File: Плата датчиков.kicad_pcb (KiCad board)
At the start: 4 copper layers, 67 x 68.5 mm, 51 parts, among them J1 A, J10 4900, J11 4900, J12 4900, J13 4900, J14 4900, J2 B, J3 C, J4 Conn_02x07_Odd_Even, J5 4900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

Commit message: Собираю документацию
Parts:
- added R15: 9.1k, Resistor_SMD:R_0603_1608Metric_Pad0.98x0.95mm_HandSolder, F.Cu at (81.5, 107.4)
- added R16: 1k, Resistor_SMD:R_0603_1608Metric_Pad0.98x0.95mm_HandSolder, F.Cu at (80.0, 107.4)
- added R17: 1k, Resistor_SMD:R_0603_1608Metric_Pad0.98x0.95mm_HandSolder, F.Cu at (80.0, 112.3)
- added R18: 1k, Resistor_SMD:R_0603_1608Metric_Pad0.98x0.95mm_HandSolder, F.Cu at (94.2, 107.2)
- added R19: 9.1k, Resistor_SMD:R_0603_1608Metric_Pad0.98x0.95mm_HandSolder, F.Cu at (92.7, 107.2)
- added R20: 9.1k, Resistor_SMD:R_0603_1608Metric_Pad0.98x0.95mm_HandSolder, F.Cu at (81.5, 112.3)
- C10, C12, C14: value 100n -> 1u
- R11, R13, R9: value 1.5k -> 15k
- moved J8 35.1 mm to (96.0, 114.6), turned to 0 degrees
- moved R14 33.8 mm to (83.3, 116.6), turned to 90 degrees
- moved C17 33.8 mm to (83.3, 116.6), turned to 90 degrees
- moved C14 31.2 mm to (85.9, 116.6), turned to -90 degrees
- moved R13 31.2 mm to (85.9, 116.6), turned to 90 degrees
- moved R3 27.0 mm to (94.0, 80.9)
- moved U1 27.0 mm to (97.5, 82.8)
- moved C16 27.0 mm to (94.0, 84.7)
- moved C15 26.8 mm to (97.0, 78.2)
- moved J9 26.3 mm to (109.7, 100.6), turned to 180 degrees
- moved R12 25.8 mm to (83.3, 105.4), turned to -90 degrees
- moved C18 24.9 mm to (85.9, 111.0), turned to -90 degrees
- moved J5 24.8 mm to (109.7, 96.3), turned to 180 degrees
- moved U4 24.7 mm to (87.1, 111.0), turned to -90 degrees
- moved R4 24.1 mm to (107.4, 88.6), turned to 0 degrees
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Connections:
- J8 pad 2: PTC_Coil_C -> GNDA
- J8 pad 3: PTC_Coil_B -> PTC_Coil_C
- J8 pad 4: GNDA -> PTC_Coil_B
- R10 pad 2: Net-(U4A--) -> Net-(R10-Pad2)
- R12 pad 2: Net-(U4B--) -> Net-(R12-Pad2)
- R14 pad 2: Net-(U4C--) -> Net-(R14-Pad2)
- U4 pad 1: Net-(U4A--) -> Net-(R10-Pad2)
- U4 pad 7: Net-(U4B--) -> Net-(R12-Pad2)
- U4 pad 8: Net-(U4C--) -> Net-(R14-Pad2)
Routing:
- net GND: track 0.00 -> 68.2 mm, vias 0 -> 4
- net +3.3VA: track 0.00 -> 51.0 mm, vias 0 -> 1
- net +3.3V: track 0.00 -> 46.8 mm, vias 0 -> 4
- net GNDA: track 0.00 -> 33.2 mm, vias 0 -> 4
- net Current_C_MCU: track 0.00 -> 33.0 mm, vias 0 -> 1
- net OUT_MCU: track 0.00 -> 28.7 mm, vias 0 -> 1
- net Temp_Coil_C_MCU: track 0.00 -> 28.4 mm, vias 0 -> 1
- net PTC_Coil_B: track 0.00 -> 24.6 mm, vias 0 -> 1
- net CS_MCU: track 0.00 -> 22.4 mm, vias 0 -> 1
- net SDIO_MCU: track 0.00 -> 22.0 mm, vias 0 -> 1
- net Current_B_MCU: track 0.00 -> 21.6 mm, vias 0 -> 1
- net SCLK_MCU: track 0.00 -> 20.2 mm, vias 0 -> 1
- net Temp_Coil_B_MCU: track 0.00 -> 18.6 mm, vias 0 -> 1
- net PTC_Coil_C: track 0.00 -> 16.1 mm, vias 0 -> 1
- net PTC_Coil_A: track 0.00 -> 15.2 mm, vias 0 -> 1
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- added copper zone on In1.Cu, net +3.3V
- added copper zone on B.Cu, net A
- added copper zone on F.Cu, net A
- added copper zone on In1.Cu, net A
- added copper zone on In2.Cu, net A
- added copper zone on B.Cu, net A_OUT
- added copper zone on F.Cu, net A_OUT
- added copper zone on In1.Cu, net A_OUT
- added copper zone on In2.Cu, net A_OUT
- added copper zone on B.Cu, net B
- added copper zone on F.Cu, net B
- added copper zone on In1.Cu, net B
- added copper zone on In2.Cu, net B
- added copper zone on B.Cu, net B_OUT
- added copper zone on F.Cu, net B_OUT
- added copper zone on In1.Cu, net B_OUT
- added copper zone on In2.Cu, net B_OUT
- added copper zone on B.Cu, net C
- added copper zone on F.Cu, net C
- added copper zone on In1.Cu, net C
- added copper zone on In2.Cu, net C
- added copper zone on B.Cu, net C_OUT
- added copper zone on F.Cu, net C_OUT
- added copper zone on In1.Cu, net C_OUT
- added copper zone on In2.Cu, net C_OUT
- added copper zone on B.Cu, net GND
- added copper zone on F.Cu, net GND
- added copper zone on In2.Cu, net GNDA

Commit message: Добавил все документы
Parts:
- moved C10 69.7 mm to (157.0, 92.7)
- moved C3 69.7 mm to (148.0, 86.5)
- moved C4 69.7 mm to (155.4, 86.5)
- moved J1 69.7 mm to (174.0, 70.5)
- moved J12 69.7 mm to (140.0, 62.1)
- moved R1 69.7 mm to (146.1, 86.5)
- moved R2 69.7 mm to (157.4, 86.5)
- moved R9 69.7 mm to (157.0, 92.7)
- moved U1 69.7 mm to (166.1, 70.1)
- moved C1 69.7 mm to (146.7, 89.1)
- moved C11 69.7 mm to (159.5, 92.7)
- moved C13 69.7 mm to (151.9, 92.7)
- moved C15 69.7 mm to (165.6, 65.5)
- moved C16 69.7 mm to (162.6, 72.0)
- moved C17 69.7 mm to (151.9, 103.9)
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
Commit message: Версия под отчёт
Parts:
- R1: value 10 -> 0
- R2: value 50 -> 51
- U1, U2, U3: value INA283 -> INA282

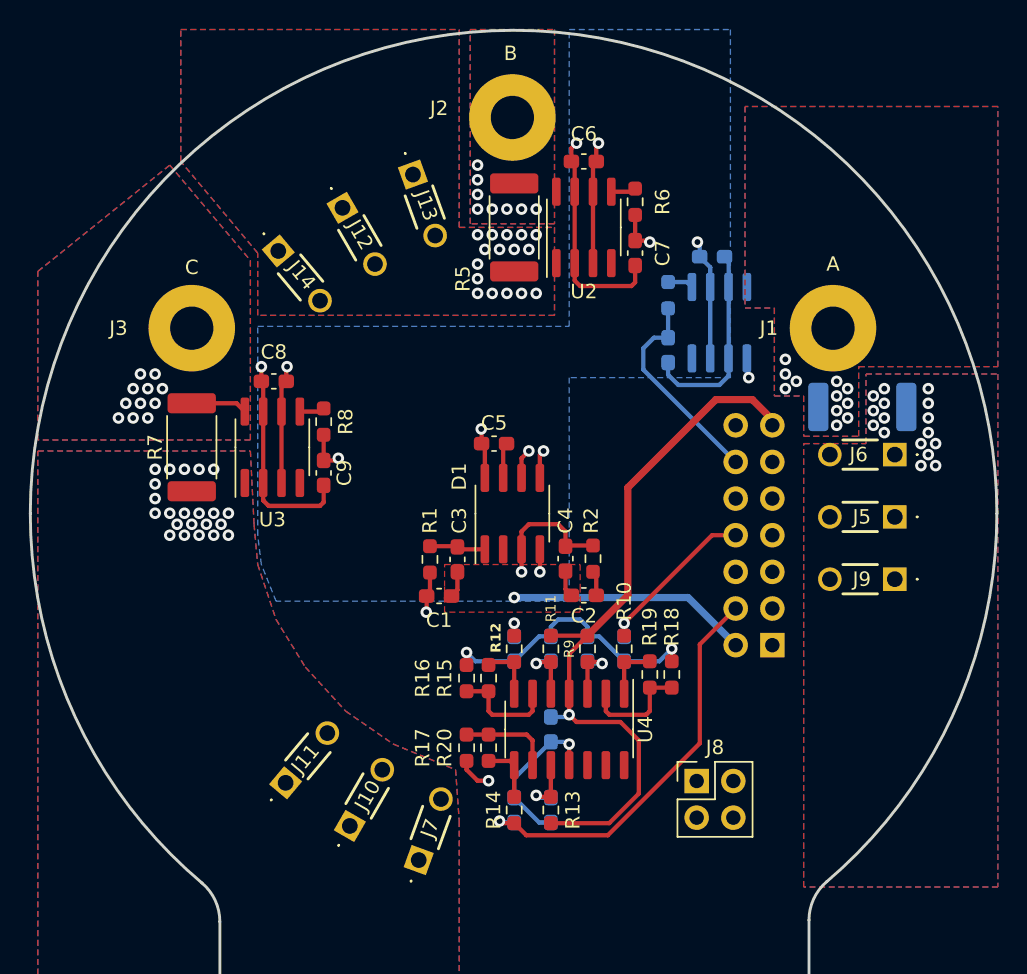
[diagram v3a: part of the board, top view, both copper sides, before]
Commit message: Изменил разводку шунтов, вывел выход датчика положения после фильтра
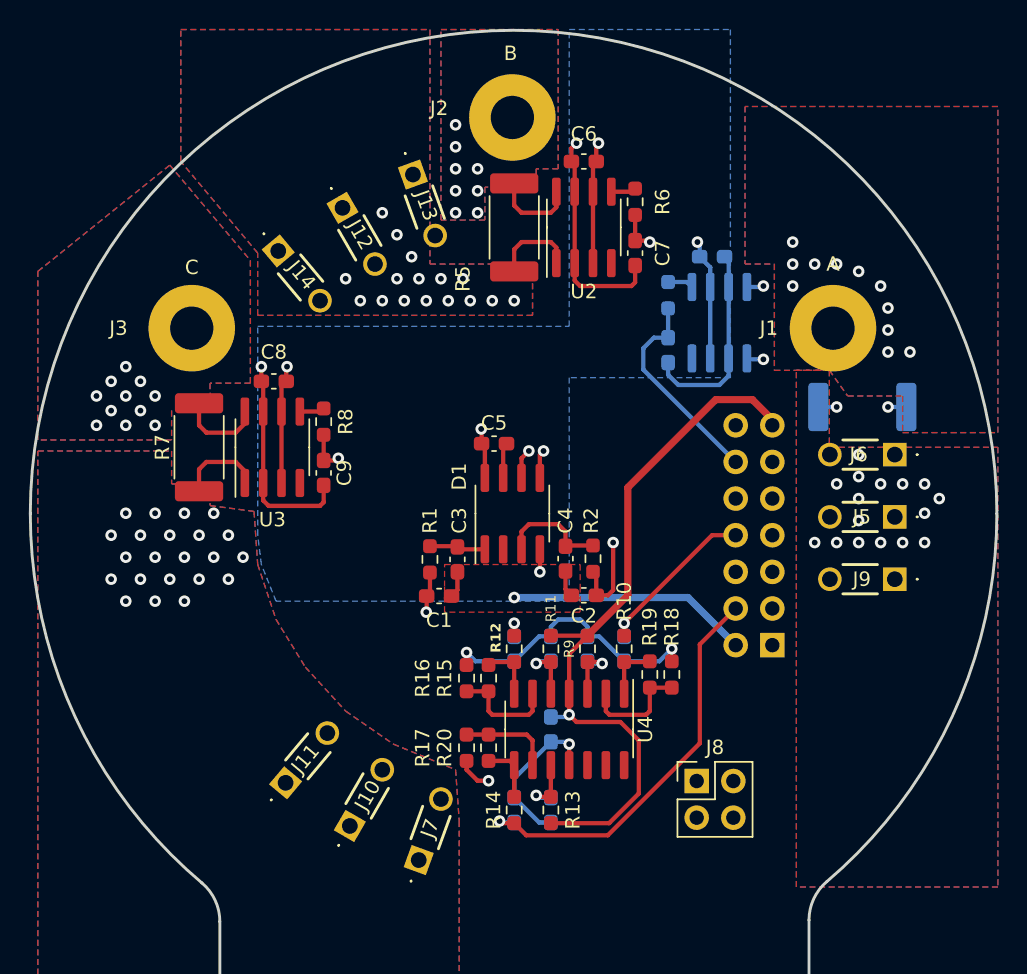
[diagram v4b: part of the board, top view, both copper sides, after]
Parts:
- moved R7 0.51 mm to (130.0, 78.7)
- turned R4 to 180 degrees
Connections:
- C2 pad 2: Net-(C2-Pad2) -> OUT_MCU
- C4 pad 2: OUT_MCU -> Net-(D1-OUT)
- D1 pad 3: OUT_MCU -> Net-(D1-OUT)
- R2 pad 1: Net-(C2-Pad2) -> OUT_MCU
- R2 pad 2: OUT_MCU -> Net-(D1-OUT)
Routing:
- net A: track 0.00 -> 16.8 mm, vias 11 -> 13
- net OUT_MCU: track 28.7 -> 18.6 mm
- net Net-(D1-OUT): track 0.00 -> 7.64 mm
- net C_OUT: track 0.00 -> 6.00 mm
- net B: track 0.00 -> 5.89 mm
- net B_OUT: track 0.00 -> 5.89 mm
- net C: track 3.92 -> 6.00 mm
- net Net-(C2-Pad2): track 1.72 -> 0.00 mm
- net SCLK_MCU: track 20.2 -> 18.7 mm
- net A_OUT: track 9.35 -> 8.89 mm, vias 17 -> 18

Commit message: VER2.0
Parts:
- removed C14: 1u, Capacitor_SMD:C_0603_1608Metric_Pad1.08x0.95mm_HandSolder
- removed C17: 100n, Capacitor_SMD:C_0603_1608Metric_Pad1.08x0.95mm_HandSolder
- removed R13: 15k, Resistor_SMD:R_0603_1608Metric_Pad0.98x0.95mm_HandSolder
- removed R14: 120, Resistor_SMD:R_0603_1608Metric_Pad0.98x0.95mm_HandSolder
- removed R17: 1k, Resistor_SMD:R_0603_1608Metric_Pad0.98x0.95mm_HandSolder
- removed R20: 9.1k, Resistor_SMD:R_0603_1608Metric_Pad0.98x0.95mm_HandSolder
- added J15: Conn_02x04_Odd_Even, Connector_PinHeader_2.00mm:PinHeader_2x04_P2.00mm_Vertical, F.Cu at (133.4, 61.5)
- added R21: 0.5m, Resistor_SMD:R_2512_6332Metric_Pad1.40x3.35mm_HandSolder, F.Cu at (173.6, 66.6)
- added R22: 0.5m, Resistor_SMD:R_2512_6332Metric_Pad1.40x3.35mm_HandSolder, F.Cu at (151.4, 51.9)
- added R23: 0.5m, Resistor_SMD:R_2512_6332Metric_Pad1.40x3.35mm_HandSolder, F.Cu at (129.0, 66.7)
- C15, C16, R3, R4, U1: moved to F.Cu
- J4: value Conn_02x07_Odd_Even -> 4900; footprint Connector_PinSocket_2.54mm:PinSocket_2x07_P2.54mm_Vertical -> Connector_My:4900; moved to F.Cu
- J8: value Conn_02x02_Odd_Even -> Temp; footprint Connector_PinHeader_2.54mm:PinHeader_2x02_P2.54mm_Vertical -> Connector_PinHeader_2.54mm:PinHeader_1x03_P2.54mm_Vertical
- moved J4 50.2 mm to (137.3, 54.1), turned to 90 degrees
- moved J7 32.3 mm to (124.9, 82.4), turned to 0 degrees
- moved J10 31.3 mm to (124.9, 77.9), turned to 0 degrees
- moved J11 30.6 mm to (124.9, 73.5), turned to 0 degrees
- moved J12 27.1 mm to (165.9, 54.1), turned to 90 degrees
- moved C16 21.8 mm to (143.3, 61.8), turned to 0 degrees
- moved R3 20.9 mm to (143.3, 60.2), turned to 0 degrees
- moved J13 17.5 mm to (161.4, 54.1), turned to 90 degrees
- moved R6 17.2 mm to (143.3, 64.0), turned to 0 degrees
- moved C7 17.0 mm to (143.2, 65.7), turned to 0 degrees
- moved C9 15.8 mm to (139.3, 64.8), turned to 90 degrees
- moved C10 13.2 mm to (150.6, 81.1)
- moved C11 13.2 mm to (153.2, 81.1)
- moved C12 13.2 mm to (148.1, 81.1)
- moved C13 13.2 mm to (145.6, 81.1)
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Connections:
- net B renamed B+
- net C renamed C+
- net C_OUT renamed C-
- C1 pad 1: +3.3V -> +3.3VA
- C1 pad 2: GND -> GNDA
- C15 pad 1: +3.3V -> +3.3VA
- C15 pad 2: GND -> GNDA
- C16 pad 2: GND -> GNDA
- C2 pad 1: GND -> GNDA
- C3 pad 2: GND -> GNDA
- C4 pad 1: GND -> GNDA
- C5 pad 1: GND -> GNDA
- C6 pad 1: +3.3V -> +3.3VA
- C6 pad 2: GND -> GNDA
- C7 pad 2: GND -> GNDA
- C8 pad 1: +3.3V -> +3.3VA
- C8 pad 2: GND -> GNDA
- C9 pad 2: GND -> GNDA
- D1 pad 4: SCLK_MCU -> unconnected-(D1-SCLK-Pad4)
- D1 pad 5: CS_MCU -> unconnected-(D1-CS-Pad5)
- D1 pad 6: SDIO_MCU -> unconnected-(D1-SDIO-Pad6)
- D1 pad 8: GND -> GNDA
- J1 pad 1: A -> A+
- J12 pad 1: B_OUT -> B-
- J12 pad 2: B_OUT -> B-
- J13 pad 1: B_OUT -> B-
- J13 pad 2: B_OUT -> B-
- J14 pad 1: B_OUT -> B-
- J14 pad 2: B_OUT -> B-
- J4 pad 1: +3.3V -> B-
- J4 pad 2: GND -> B-
- J5 pad 1: A_OUT -> A-
- J5 pad 2: A_OUT -> A-
- J6 pad 1: A_OUT -> A-
- J6 pad 2: A_OUT -> A-
- J8 pad 2: GNDA -> PTC_Coil_B
- J8 pad 3: PTC_Coil_C -> GNDA
- J9 pad 1: A_OUT -> A-
- J9 pad 2: A_OUT -> A-
- R1 pad 1: +3.3V -> +3.3VA
- R4 pad 1: A -> A-
- R4 pad 2: A_OUT -> A+
- R5 pad 2: B_OUT -> B-
- U1 pad 1: A_OUT -> A+
- U1 pad 2: GND -> GNDA
- U1 pad 3: +3.3V -> +3.3VA
- U1 pad 6: +3.3V -> +3.3VA
- U1 pad 7: GND -> GNDA
- U1 pad 8: A -> A-
- U2 pad 1: B_OUT -> B-
- U2 pad 2: GND -> GNDA
- U2 pad 3: +3.3V -> +3.3VA
- U2 pad 6: +3.3V -> +3.3VA
- U2 pad 7: GND -> GNDA
- U3 pad 2: GND -> GNDA
- U3 pad 3: +3.3V -> +3.3VA
- U3 pad 6: +3.3V -> +3.3VA
- U3 pad 7: GND -> GNDA
- U4 pad 10: PTC_Coil_C -> unconnected-(U4C-+-Pad10)
- U4 pad 12: (no net) -> unconnected-(U4D-+-Pad12)
- U4 pad 13: (no net) -> unconnected-(U4D---Pad13)
- U4 pad 14: (no net) -> unconnected-(U4-Pad14)
- U4 pad 8: Net-(R14-Pad2) -> unconnected-(U4-Pad8)
- U4 pad 9: Net-(U4C--) -> unconnected-(U4C---Pad9)
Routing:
- net GND: track 68.2 -> 0.00 mm, vias 4 -> 0
- net +3.3V: track 46.8 -> 0.00 mm, vias 4 -> 0
- net Temp_Coil_C_MCU: track 28.4 -> 0.00 mm, vias 1 -> 0
- net Net-(R6-Pad2): track 1.74 -> 28.0 mm
- net CS_MCU: track 22.4 -> 0.00 mm, vias 1 -> 0
- net SDIO_MCU: track 22.0 -> 0.00 mm, vias 1 -> 0
- net Current_C_MCU: track 33.0 -> 11.6 mm
- net Net-(R3-Pad2): track 1.79 -> 22.3 mm, vias 0 -> 2
- net GNDA: track 33.2 -> 53.1 mm, vias 4 -> 12
- net SCLK_MCU: track 18.7 -> 0.00 mm, vias 1 -> 0
- net OUT_MCU: track 18.6 -> 36.9 mm
- net Temp_Coil_A_MCU: track 11.1 -> 29.3 mm
- net A: track 16.8 -> 0.00 mm, vias 13 -> 0
- net PTC_Coil_C: track 16.1 -> 0.00 mm, vias 1 -> 0
- net B-: track 0.00 -> 14.1 mm, vias 0 -> 128
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- added copper zone on In2.Cu, net +3.3VA
- added copper zone on B.Cu, net A+
- added copper zone on F.Cu, net A+
- added copper zone on In1.Cu, net A+
- added copper zone on In2.Cu, net A+
- added copper zone on B.Cu, net A-
- added copper zone on F.Cu, net A-
- added copper zone on In1.Cu, net A-
- added copper zone on In2.Cu, net A-
- added copper zone on B.Cu, net B-
- added copper zone on F.Cu, net B-
- added copper zone on In1.Cu, net B-
- added copper zone on In2.Cu, net B-
- added copper zone on B.Cu, net GNDA
- removed copper zone on In1.Cu, net +3.3V
- removed copper zone on B.Cu, net A
- removed copper zone on F.Cu, net A
- removed copper zone on In1.Cu, net A
- removed copper zone on In2.Cu, net A
- removed copper zone on B.Cu, net A_OUT
- removed copper zone on F.Cu, net A_OUT
- removed copper zone on In1.Cu, net A_OUT
- removed copper zone on In2.Cu, net A_OUT
- removed copper zone on B.Cu, net B_OUT
- removed copper zone on F.Cu, net B_OUT
- removed copper zone on In1.Cu, net B_OUT
- removed copper zone on In2.Cu, net B_OUT
- removed copper zone on B.Cu, net GND
- removed copper zone on F.Cu, net GND
- removed copper zone on In2.Cu, net GNDA
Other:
- board size 67 x 68.5 mm -> 67 x 67 mm

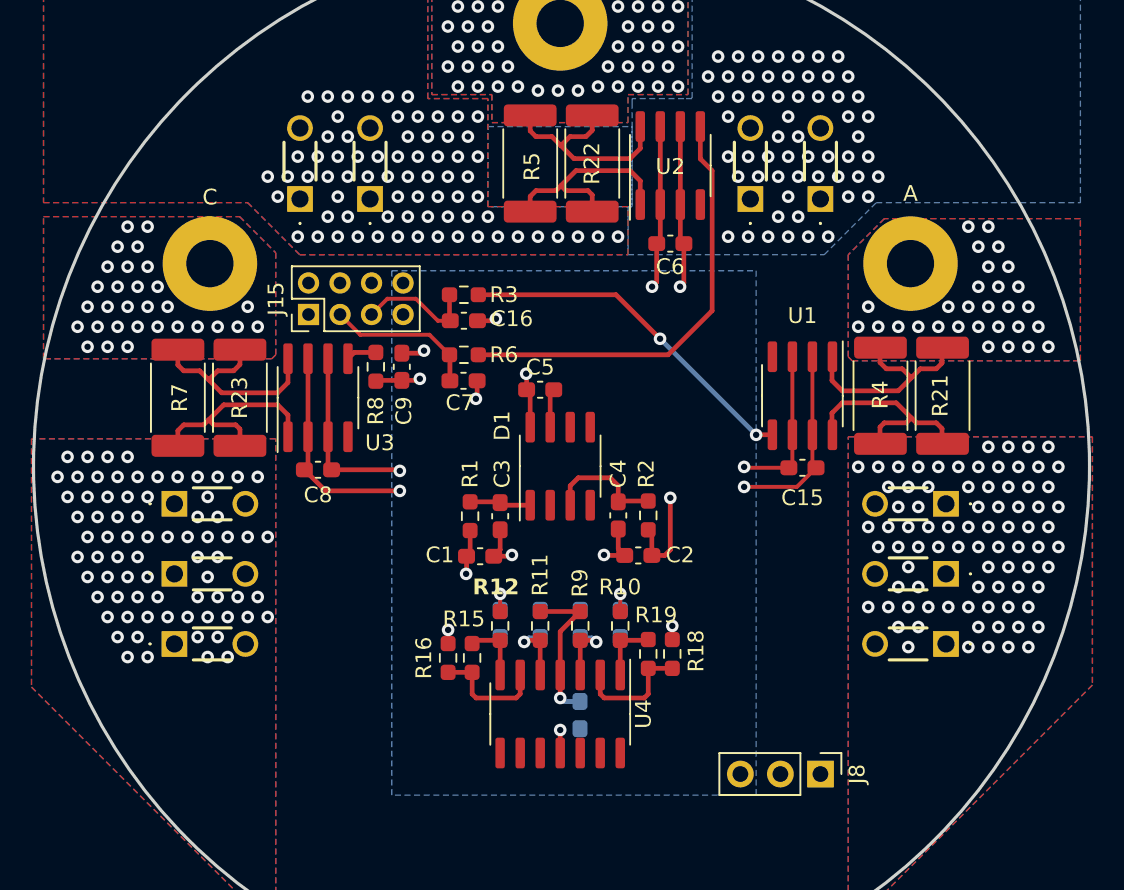
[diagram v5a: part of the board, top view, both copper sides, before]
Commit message: Убрал лишние шунты
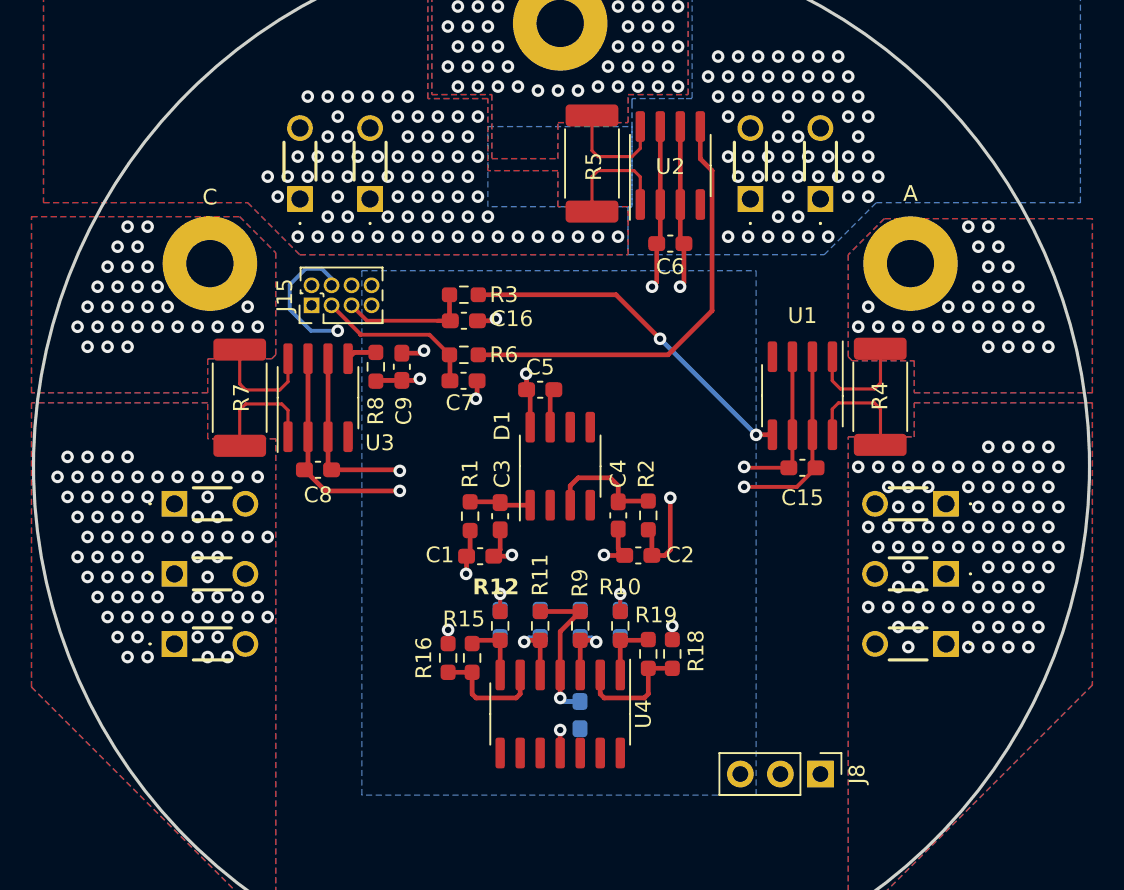
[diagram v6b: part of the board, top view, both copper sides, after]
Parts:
- removed R21, R22, R23: 0.5m, Resistor_SMD:R_2512_6332Metric_Pad1.40x3.35mm_HandSolder
- J15: footprint Connector_PinHeader_2.00mm:PinHeader_2x04_P2.00mm_Vertical -> Connector_PinHeader_1.27mm:PinHeader_2x04_P1.27mm_Vertical
- moved R7 3.92 mm to (129.0, 66.7)
- moved R5 3.92 mm to (151.4, 51.9)
- moved J15 0.61 mm to (133.6, 60.9)
- moved R4 0.07 mm to (169.7, 66.7)
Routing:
- net B+: track 14.0 -> 7.06 mm
- net A+: track 13.8 -> 7.06 mm
- net C+: track 13.8 -> 7.06 mm
- net B-: track 14.1 -> 7.36 mm
- net Temp_Coil_B_MCU: track 27.6 -> 33.9 mm, vias 1 -> 2
- net A-: track 13.6 -> 7.36 mm
- net C-: track 13.6 -> 7.36 mm
- net Temp_Coil_A_MCU: track 29.3 -> 31.1 mm
- net Current_A_MCU: track 7.66 -> 9.13 mm
- net Current_C_MCU: track 11.6 -> 12.5 mm
- net Current_B_MCU: track 9.67 -> 10.5 mm
